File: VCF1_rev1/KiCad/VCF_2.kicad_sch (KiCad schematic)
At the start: 27 parts, among them U10 CEM3350, U11 Opamp_Quad, U12 74HC4053, U9 74HC4053

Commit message: Started to populate the PCB and done some small fixes in the schematics.
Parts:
- removed U9: 74HC4053, symbol Modular_Mayhem:74HC4053
- added U8: 74HC4053, Package_SO:SOIC-16_3.9x9.9mm_P1.27mm, symbol Modular_Mayhem:74HC4053
- C11: renamed from C9; footprint (none) -> Capacitor_SMD:C_0603_1608Metric
- C12: renamed from C10; footprint (none) -> Capacitor_SMD:C_0603_1608Metric
- C13: renamed from C11; footprint (none) -> Capacitor_SMD:C_0603_1608Metric
- D10, D11, D12, D9: footprint (none) -> Diode_SMD:D_SOD-123
- U10: renamed from U11; footprint (none) -> Package_SO:SOIC-14_3.9x8.7mm_P1.27mm
- U2: renamed from U12; footprint (none) -> Package_SO:SOIC-16_3.9x9.9mm_P1.27mm
- U9: renamed from U10; footprint (none) -> Package_SO:SOIC-16_3.9x9.9mm_P1.27mm
- renumbered R66 to R69, R67 to R70, R68 to R71, R69 to R72, R70 to R73, R71 to R74, R72 to R75, R73 to R76, R74 to R77, R75 to R78, R76 to R79, R77 to R80, R78 to R81, R79 to R82, R80 to R83, R81 to R84
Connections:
- net Audio_in: now also U8.12 (X0)
- net Audio_out: now also U10.7; no longer U10.8
- net GND: now also R70.1; no longer R70.2
- net HP_select: now also U8.9 (C)
- net Invert_select: now also U8.10 (B)
- net LP_select: now also U8.13 (X1)
- net Overdrive_select: now also U2.9 (C); no longer U2.11 (A)
- net VCF2_HP_out: now also U10.8, U8.3 (Z1); no longer U10.7
- net VCF2_LP_BP_out: now also R77.1, U10.14, U8.5 (Z0); no longer R77.2, U10.1
- net at R81.1: now also U8.2 (Y0), U8.4 (Z)
- net at D10.2 (A), D9.1 (K), R74.1: now also C13.2; no longer C13.1
- net at R84.1: now also U2.5 (Z0); no longer U2.12 (X0)
- net at C12.1, U9.5 (Vbp): now also C11.1, U10.10 (+); no longer C11.2, U10.5 (+)
- net at U9.6 (Vcq): now also R70.2; no longer R70.1
- net at R82.1: now also U10.5 (+), U8.15 (Y); no longer U10.10 (+)
- net at R71.1: now also U8.11 (A)
- net at R76.1, R78.1: now also U10.9 (-); no longer U10.6 (-)
- net at D11.2 (A), D12.1 (K): now also U2.3 (Z1); no longer U2.13 (X1)
- new net: C11.2, U8.14 (X)
- new net: C13.1, U10.12 (+), U9.3 (Vlp)
- new net: R75.1, R77.2, U10.13 (-)
- new net: U10.6 (-), U2.4 (Z)
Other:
- moved on the sheet: C11, C13, R70, R77

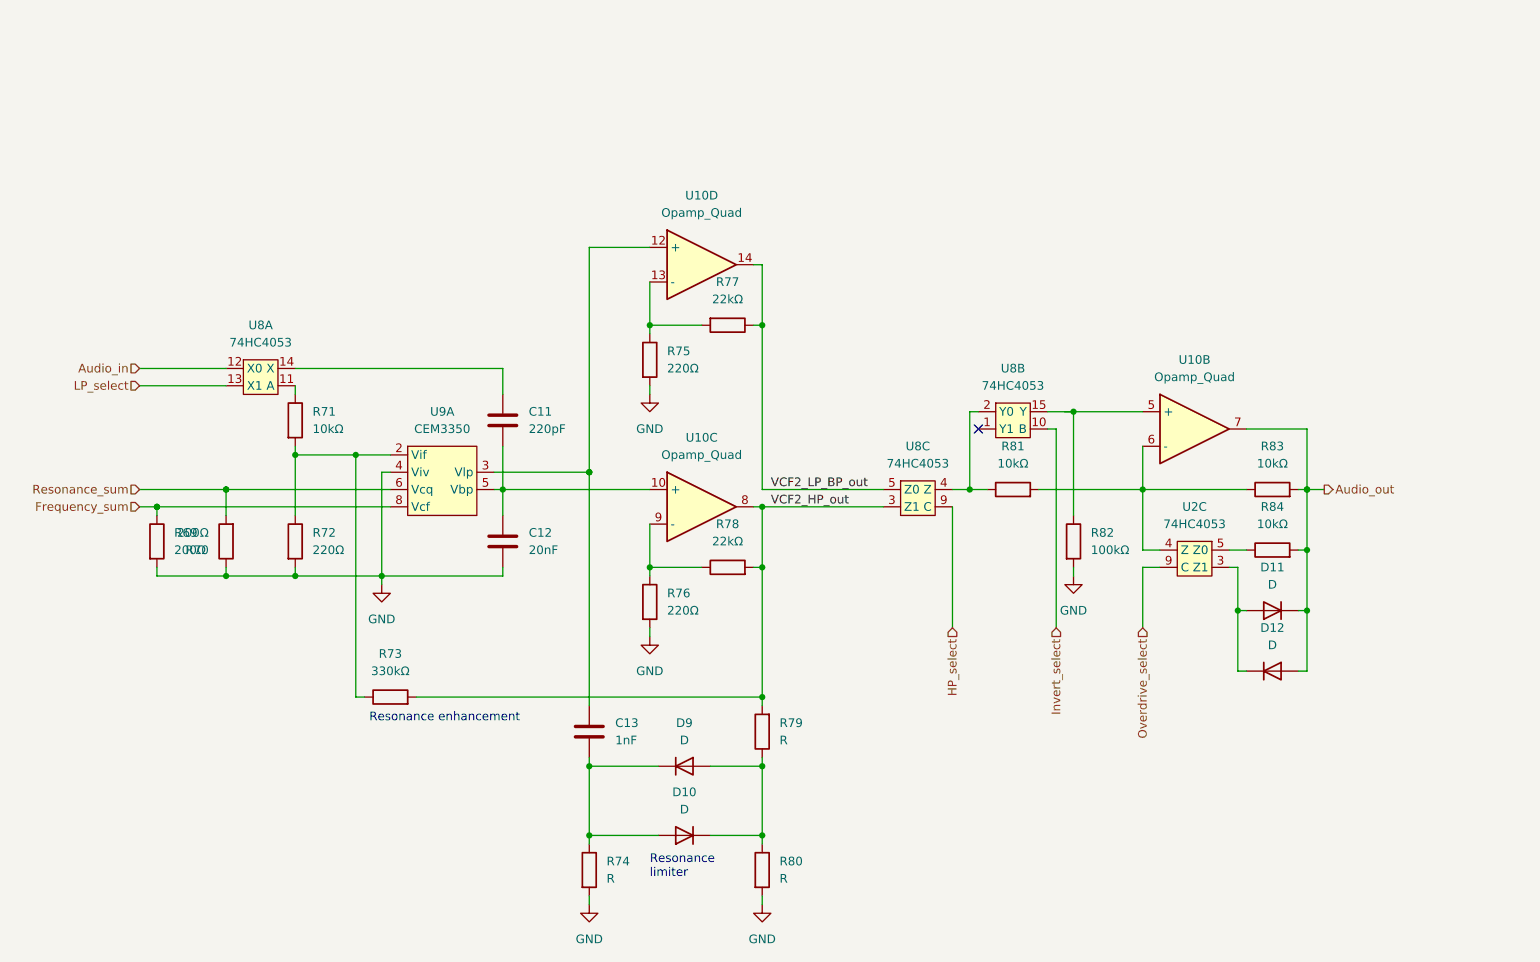
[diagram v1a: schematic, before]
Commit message: Placed more components on the PCB.
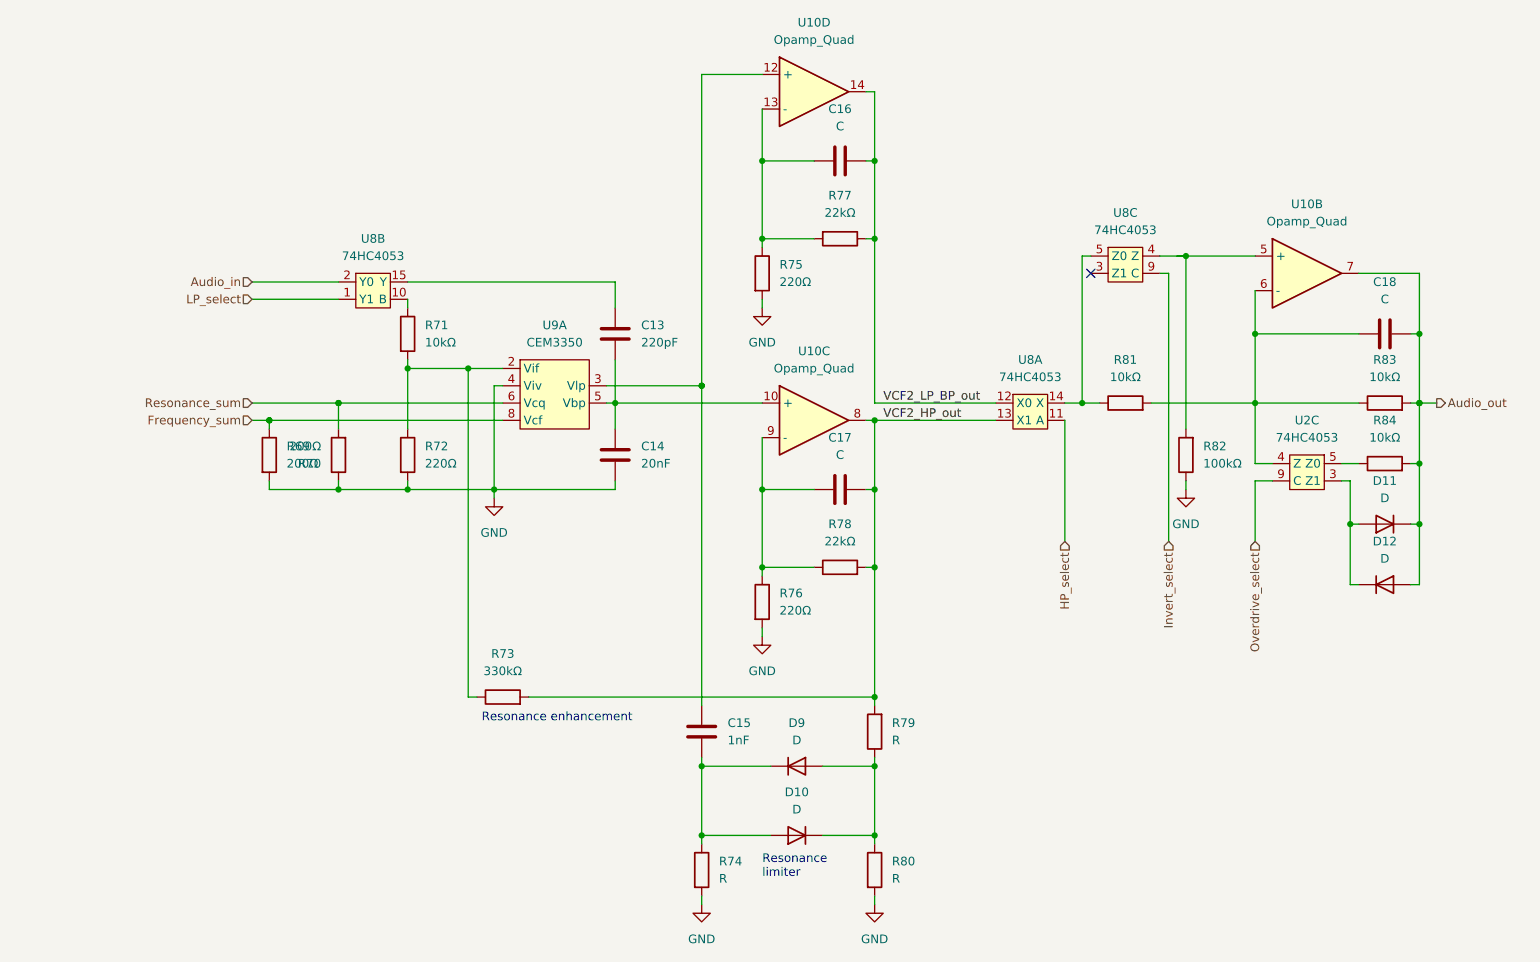
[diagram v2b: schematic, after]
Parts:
- added C16, C17, C18: C, Capacitor_SMD:C_0603_1608Metric, symbol Device:C
- renumbered C11 to C13, C12 to C14, C13 to C15
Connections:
- net Audio_in: now also U8.2 (Y0); no longer U8.12 (X0)
- net Audio_out: now also C18.1
- net GND: now also R82.1; no longer R82.2
- net HP_select: now also U8.11 (A); no longer U8.9 (C)
- net Invert_select: now also U8.9 (C); no longer U8.10 (B)
- net LP_select: now also U8.1 (Y1); no longer U8.13 (X1)
- net VCF2_HP_out: now also U8.13 (X1), C17.2; no longer U8.3 (Z1)
- net VCF2_LP_BP_out: now also U8.12 (X0), C16.1; no longer U8.5 (Z0)
- net at R71.1: now also U8.10 (B); no longer U8.11 (A)
- net at C13.2: now also U8.15 (Y); no longer U8.14 (X)
- net at R76.1, R78.1, U10.9 (-): now also C17.1
- net at R75.1, R77.2, U10.13 (-): now also C16.2
- net at U10.6 (-), U2.4 (Z): now also C18.2
- new net: R81.1, U8.14 (X), U8.5 (Z0)
- new net: R82.2, U10.5 (+), U8.4 (Z)
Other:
- moved on the sheet: C13, C14, C15, D10, D11, D12, D9, R69, R70, R71, R72, R73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
